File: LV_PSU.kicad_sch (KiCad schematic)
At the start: 20 parts, among them J3 1935161, J5 Header_Male_Pin_2.54mm_1X2_,_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, U2 OKI-78SR-5_1.5-W36H-C, U3 AZ1117IH-3.3TRG1

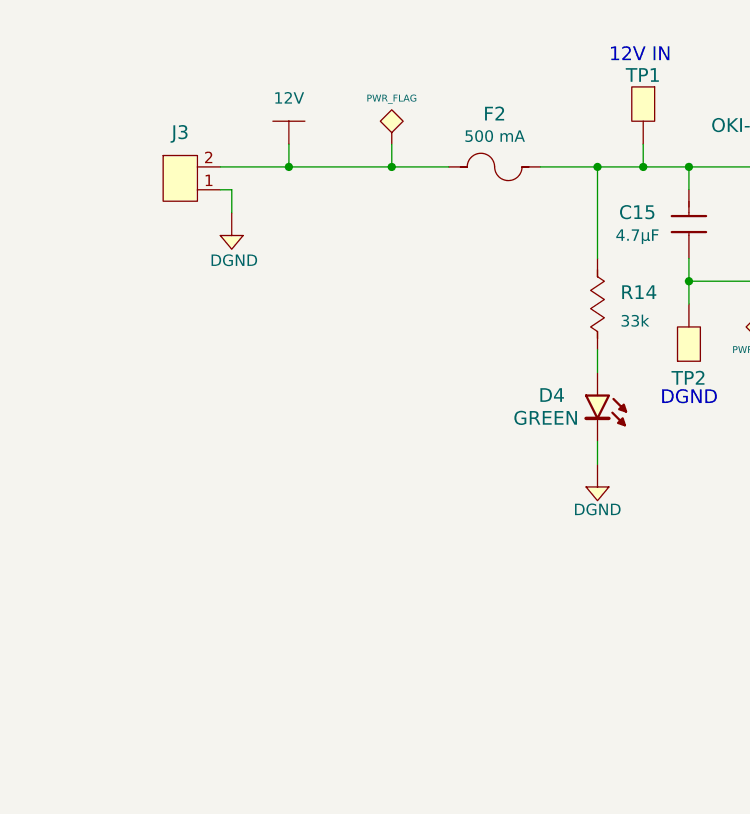
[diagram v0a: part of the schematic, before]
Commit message: update schematic
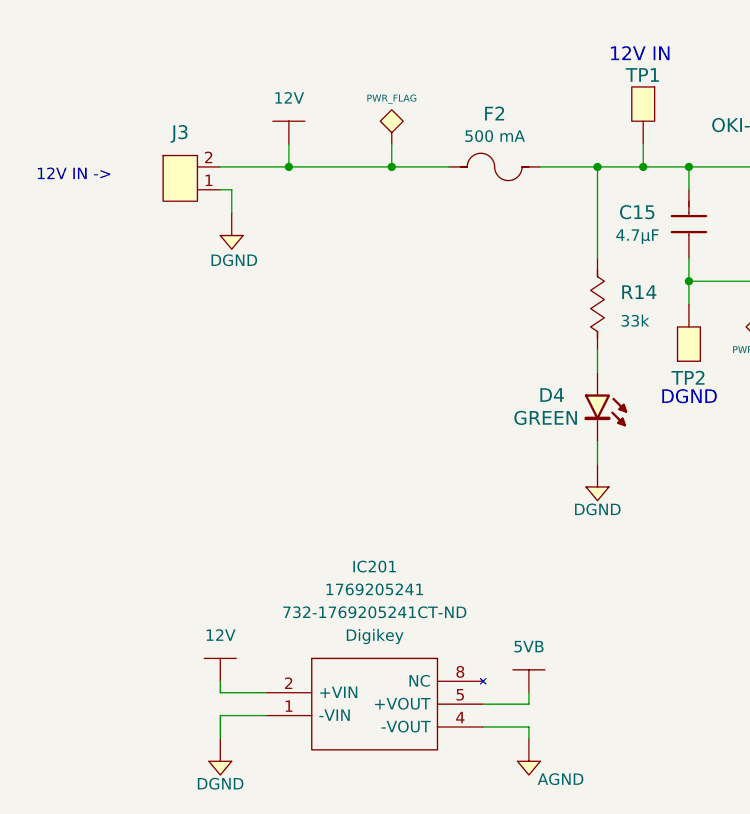
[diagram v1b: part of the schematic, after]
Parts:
- added IC201: 1769205241, IC:1769205241, symbol PMIC:1769205241
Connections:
- net 12V: now also IC201.2 (+VIN)
- net DGND: now also IC201.1 (-VIN)
- new net 5VB: IC201.5 (+VOUT)
- new net AGND: IC201.4 (-VOUT)
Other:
- note added: "12V IN ->"

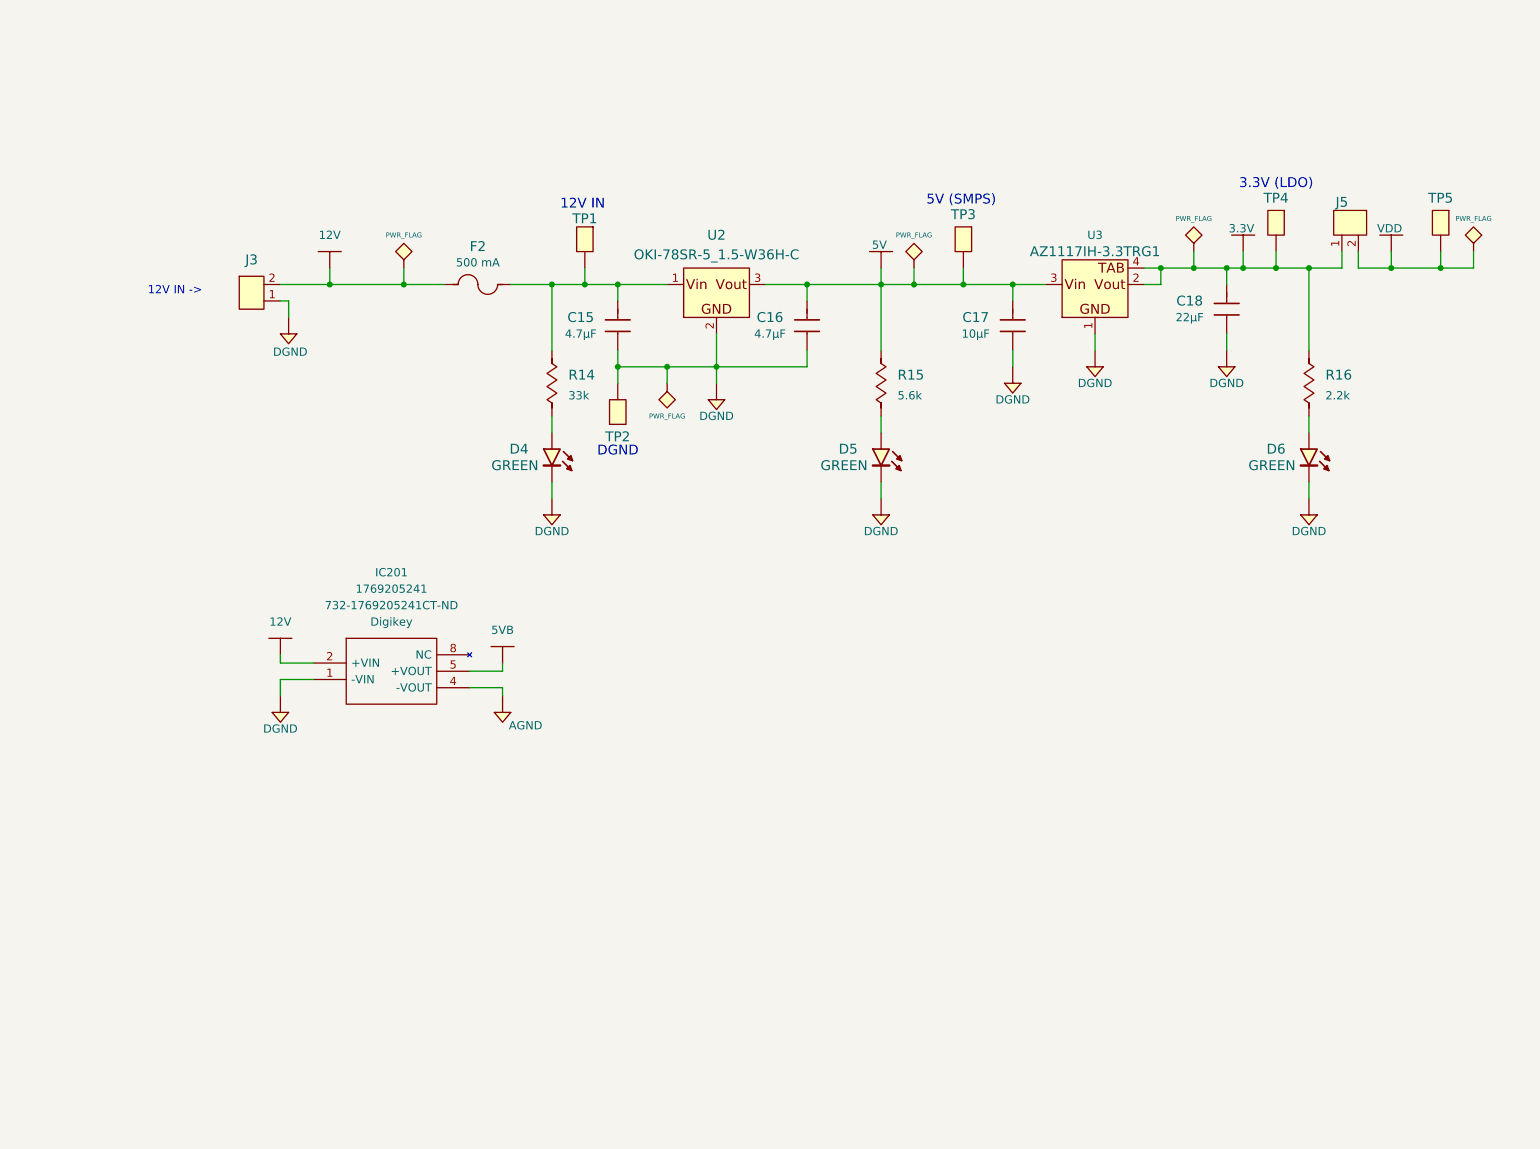
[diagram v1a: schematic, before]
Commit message: update schematic
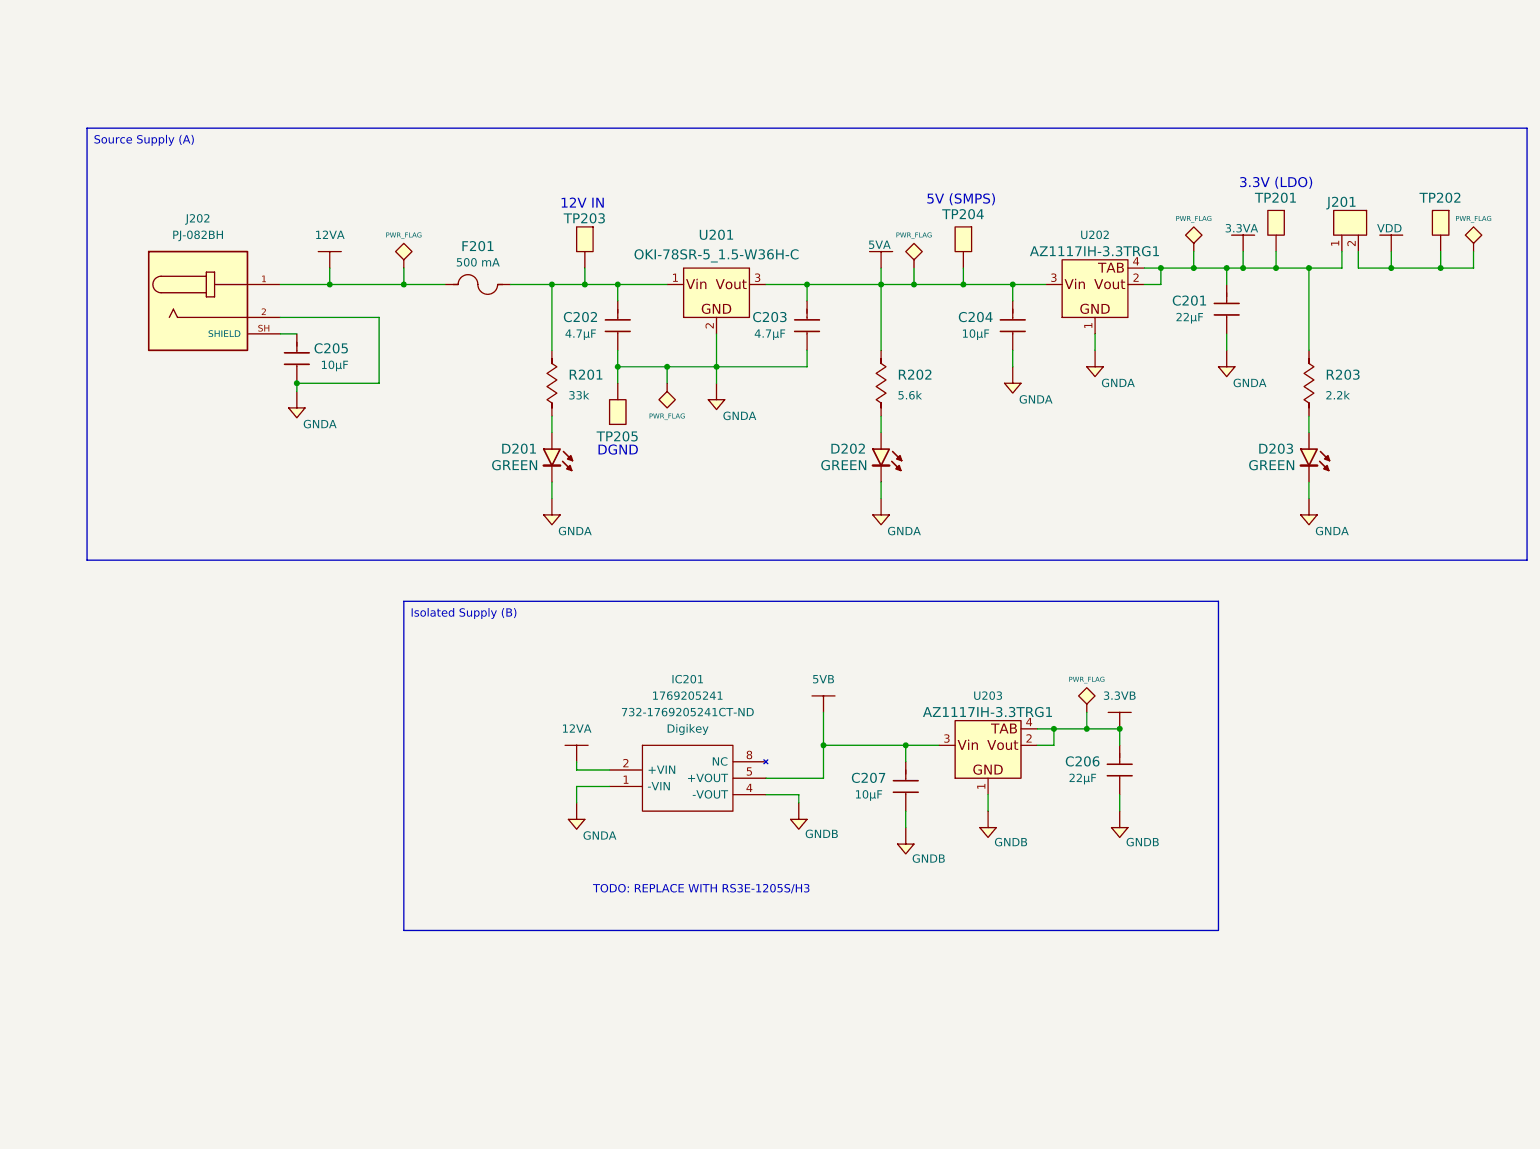
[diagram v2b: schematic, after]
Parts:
- removed J3: 1935161, Connectors:1935161, symbol Connectors:1935161
- added C205, C207: 885012107014, Capacitors:C0805, symbol Capacitors:885012107014
- added C206: 885012107005, Capacitors:C0805, symbol Capacitors:885012107005
- added J202: PJ-082BH, Connectors:CUI_PJ-082BH, symbol Connectors:PJ-082BH
- added U203: AZ1117IH-3.3TRG1, IC:SOT-223-3, symbol PMIC:AZ1117IH-3.3TRG1
- renumbered C18 to C201, C15 to C202, C16 to C203, C17 to C204, D4 to D201, D5 to D202, D6 to D203, F2 to F201, J5 to J201, R14 to R201, R15 to R202, R16 to R203, TP4 to TP201, TP5 to TP202, TP1 to TP203, TP3 to TP204, TP2 to TP205, U2 to U201, U3 to U202
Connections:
- net 5VB: now also C207.2, U203.3 (Vin)
- net 12V renamed 12VA
- net 12VA: now also J202.1
- net 3.3V renamed 3.3VA
- net 5V renamed 5VA
- net AGND renamed GNDB
- net GNDB: now also C206.1, C207.1, U203.1 (GND)
- net DGND renamed GNDA
- net GNDA: now also C205.1, J202.2
- new net: C205.2, J202.SH (SHIELD)
- new net 3.3VB: C206.2, U203.2 (Vout), U203.4 (Vout_(TAB))
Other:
- note added: "TODO: REPLACE WITH RS3E-1205S/H3"
- note removed: "12V IN ->"
- moved on the sheet: IC201

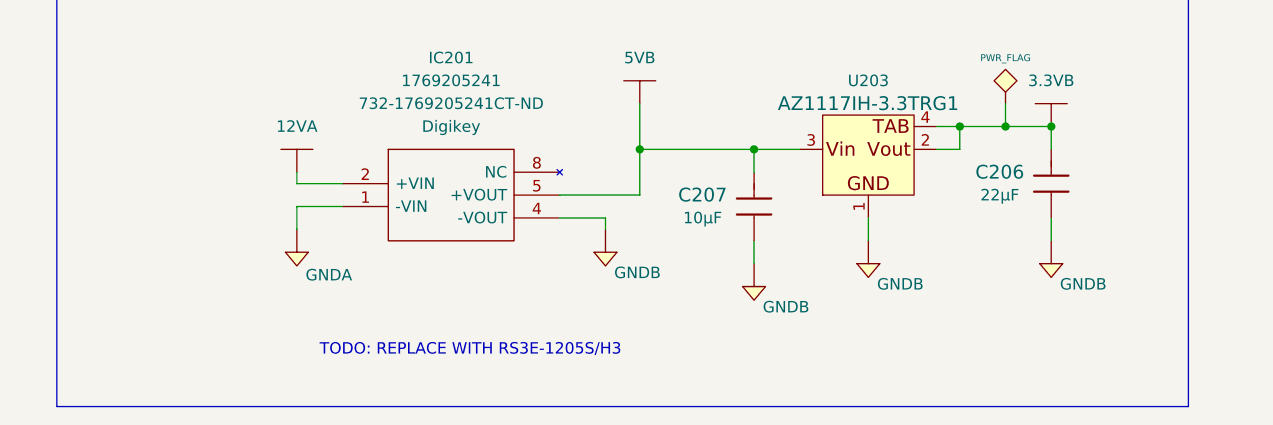
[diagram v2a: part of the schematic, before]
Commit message: update schematic
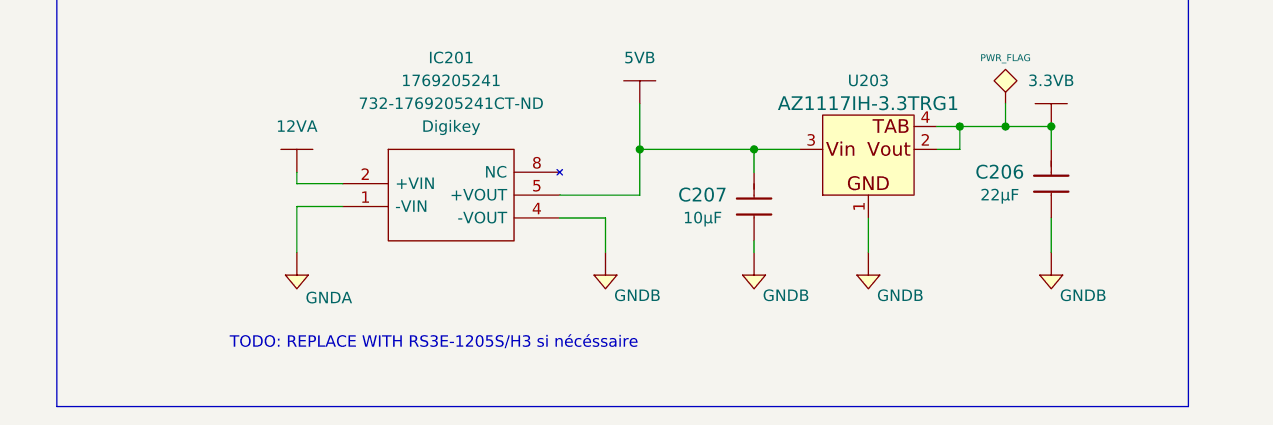
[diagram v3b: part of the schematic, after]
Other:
- note added: "TODO: REPLACE WITH RS3E-1205S/H3 si nécéssaire"
- note removed: "TODO: REPLACE WITH RS3E-1205S/H3"
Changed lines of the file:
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@@
 	(wire
 		(pts
-			(xy 111.76 138.43) (xy 111.76 135.89)
+			(xy 111.76 140.97) (xy 111.76 135.89)
 		)
 		(stroke
@@
 	(wire
 		(pts
-			(xy 146.05 138.43) (xy 146.05 137.16)
+			(xy 146.05 140.97) (xy 146.05 137.16)
 		)
 		(stroke
@@
 	(wire
 		(pts
-			(xy 175.26 137.16) (xy 175.26 139.7)
+			(xy 175.26 137.16) (xy 175.26 140.97)
 		)
 		(stroke
@@
 	(wire
 		(pts
-			(xy 162.56 139.7) (xy 162.56 142.24)
+			(xy 162.56 139.7) (xy 162.56 140.97)
 		)
 		(stroke
@@
 	(wire
 		(pts
-			(xy 195.58 137.16) (xy 195.58 139.7)
+			(xy 195.58 137.16) (xy 195.58 140.97)
 		)
 		(stroke
@@
 		)
 	)
-	(text "TODO: REPLACE WITH RS3E-1205S/H3"
+	(text "TODO: REPLACE WITH RS3E-1205S/H3 si nécéssaire"
 		(exclude_from_sim no)
-		(at 131.064 151.892 0)
+		(at 127 151.13 0)
 		(effects
 			(font
@@
 	(symbol
 		(lib_id "Power_Port:GNDB")
-		(at 146.05 140.97 0)
+		(at 146.05 143.51 0)
 		(unit 1)
 		(exclude_from_sim no)
@@
 		(dnp no)
 		(property "Reference" "#PWR0217"
-			(at 146.05 145.288 0)
+			(at 146.05 147.828 0)
 			(effects
 				(font
@@
 		)
 		(property "Value" "GNDB"
-			(at 149.606 143.256 0)
+			(at 149.606 145.796 0)
 			(effects
 				(font
@@
 		)
 		(property "Footprint" ""
-			(at 146.05 138.43 0)
+			(at 146.05 140.97 0)
 			(effects
 				(font
@@
 		)
 		(property "Datasheet" ""
-			(at 145.542 143.256 0)
+			(at 145.542 145.796 0)
 			(effects
 				(font
@@
 		)
 		(property "Description" ""
-			(at 146.05 140.97 0)
+			(at 146.05 143.51 0)
 			(effects
 				(font
@@
 	(symbol
 		(lib_id "Power_Port:GNDB")
-		(at 175.26 142.24 0)
+		(at 175.26 143.51 0)
 		(unit 1)
 		(exclude_from_sim no)
@@
 		(dnp no)
 		(property "Reference" "#PWR0218"
-			(at 175.26 146.558 0)
+			(at 175.26 147.828 0)
 			(effects
 				(font
@@
 		)
 		(property "Value" "GNDB"
-			(at 178.816 144.526 0)
+			(at 178.816 145.796 0)
 			(effects
 				(font
@@
 		)
 		(property "Footprint" ""
-			(at 175.26 139.7 0)
+			(at 175.26 140.97 0)
 			(effects
 				(font
@@
 		)
 		(property "Datasheet" ""
-			(at 174.752 144.526 0)
+			(at 174.752 145.796 0)
 			(effects
 				(font
@@
 		)
 		(property "Description" ""
-			(at 175.26 142.24 0)
+			(at 175.26 143.51 0)
 			(effects
 				(font
@@
 	(symbol
 		(lib_id "Power_Port:GNDA")
-		(at 111.76 140.97 0)
+		(at 111.76 143.51 0)
 		(unit 1)
 		(exclude_from_sim no)
@@
 		(dnp no)
 		(property "Reference" "#PWR0216"
-			(at 111.76 145.288 0)
+			(at 111.76 147.828 0)
 			(effects
 				(font
@@
 		)
 		(property "Value" "GNDA"
-			(at 115.316 143.51 0)
+			(at 115.316 146.05 0)
 			(effects
 				(font
@@
 		)
 		(property "Footprint" ""
-			(at 111.76 138.43 0)
+			(at 111.76 140.97 0)
 			(effects
 				(font
@@
 		)
 		(property "Datasheet" ""
-			(at 111.252 143.256 0)
+			(at 111.252 145.796 0)
 			(effects
 				(font
@@
 		)
 		(property "Description" ""
-			(at 111.76 140.97 0)
+			(at 111.76 143.51 0)
 			(effects
 				(font
@@
 	(symbol
 		(lib_id "Power_Port:GNDB")
-		(at 195.58 142.24 0)
+		(at 195.58 143.51 0)
 		(unit 1)
 		(exclude_from_sim no)
@@
 		(dnp no)
 		(property "Reference" "#PWR0219"
-			(at 195.58 146.558 0)
+			(at 195.58 147.828 0)
 			(effects
 				(font
@@
 		)
 		(property "Value" "GNDB"
-			(at 199.136 144.526 0)
+			(at 199.136 145.796 0)
 			(effects
 				(font
@@
 		)
 		(property "Footprint" ""
-			(at 195.58 139.7 0)
+			(at 195.58 140.97 0)
 			(effects
 				(font
@@
 		)
 		(property "Datasheet" ""
-			(at 195.072 144.526 0)
+			(at 195.072 145.796 0)
 			(effects
 				(font
@@
 		)
 		(property "Description" ""
-			(at 195.58 142.24 0)
+			(at 195.58 143.51 0)
 			(effects
 				(font
@@
 	(symbol
 		(lib_id "Power_Port:GNDB")
-		(at 162.56 144.78 0)
+		(at 162.56 143.51 0)
 		(unit 1)
 		(exclude_from_sim no)
@@
 		(dnp no)
 		(property "Reference" "#PWR0220"
-			(at 162.56 149.098 0)
+			(at 162.56 147.828 0)
 			(effects
 				(font
@@
 		)
 		(property "Value" "GNDB"
-			(at 166.116 147.066 0)
+			(at 166.116 145.796 0)
 			(effects
 				(font
@@
 		)
 		(property "Footprint" ""
-			(at 162.56 142.24 0)
+			(at 162.56 140.97 0)
 			(effects
 				(font
@@
 		)
 		(property "Datasheet" ""
-			(at 162.052 147.066 0)
+			(at 162.052 145.796 0)
 			(effects
 				(font
@@
 		)
 		(property "Description" ""
-			(at 162.56 144.78 0)
+			(at 162.56 143.51 0)
 			(effects
 				(font
